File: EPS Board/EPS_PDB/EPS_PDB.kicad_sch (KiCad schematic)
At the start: 2 parts, among them J1 Conn_02x26_Odd_Even, J2 Conn_02x26_Odd_Even

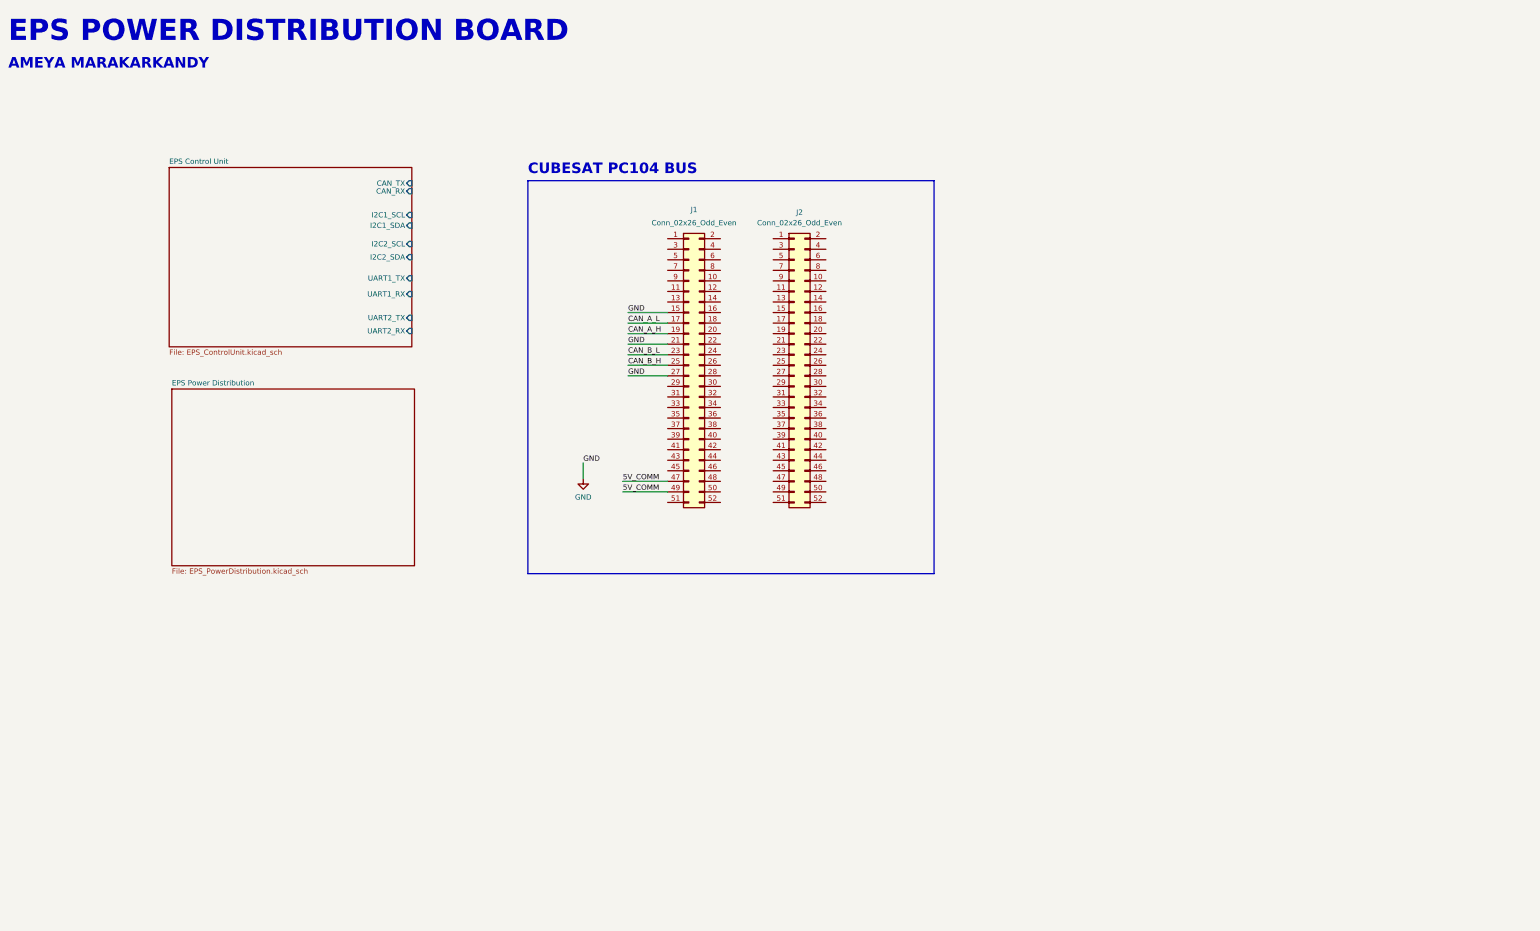
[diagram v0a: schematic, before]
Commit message: EPS PDB Board Schematic progress
Interfaces defined in EPS PDB board Schematic
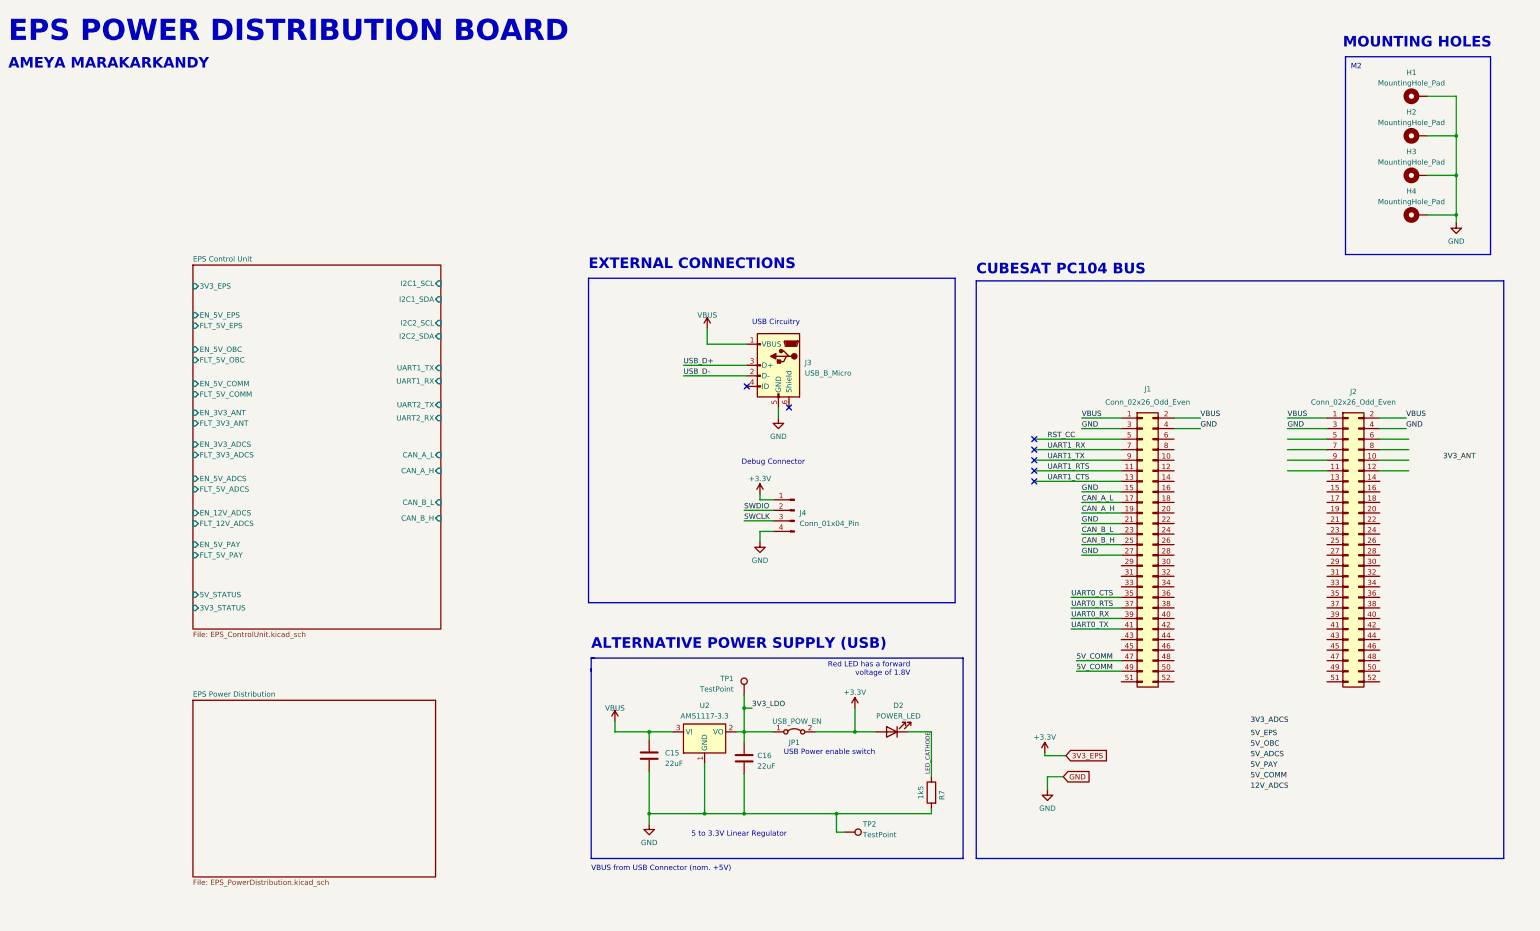
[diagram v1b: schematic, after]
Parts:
- added C15, C16: 22uF, symbol Device:C
- added D2: POWER_LED, symbol Device:LED
- added H1, H2, H3, H4: MountingHole_Pad, symbol Mechanical:MountingHole_Pad
- added J3: USB_B_Micro, symbol Connector:USB_B_Micro
- added J4: Conn_01x04_Pin, symbol Connector:Conn_01x04_Pin
- added JP1: USB_POW_EN, symbol Jumper:Jumper_2_Bridged
- added R7: 1k5, symbol Device:R
- added TP1, TP2: TestPoint, symbol Connector:TestPoint
- added U2: AMS1117-3.3, symbol Regulator_Linear:AMS1117-3.3
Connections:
- net GND: now also J1.3 (Pin_3), J1.4 (Pin_4), J2.3 (Pin_3), J2.4 (Pin_4), C15.2, C16.2, H1.1, H2.1, H3.1, H4.1, J3.5 (GND), J4.4 (Pin_4), R7.2, TP2.1, U2.1 (GND)
- net VBUS: now reaches J1.1 (Pin_1)
- net VBUS: now also J1.2 (Pin_2), J2.1 (Pin_1), J2.2 (Pin_2), C15.1, J3.1 (VBUS), U2.3 (VI)
- net UART1_RTS: now reaches J1.11 (Pin_11)
- net UART1_CTS: now reaches J1.13 (Pin_13)
- net UART0_CTS: now reaches J1.35 (Pin_35)
- net UART0_RTS: now reaches J1.37 (Pin_37)
- net UART0_RX: now reaches J1.39 (Pin_39)
- net UART0_TX: now reaches J1.41 (Pin_41)
- net RST_CC: now reaches J1.5 (Pin_5)
- net UART1_RX: now reaches J1.7 (Pin_7)
- net UART1_TX: now reaches J1.9 (Pin_9)
- new net +3.3V: D2.2 (A), J4.1 (Pin_1), JP1.2 (B)
- new net 3V3_LDO: C16.1, JP1.1 (A), TP1.1, U2.2 (VO)
- new net LED_CATHODE: D2.1 (K), R7.1
- new net SWCLK: J4.3 (Pin_3)
- new net SWDIO: J4.2 (Pin_2)
- new net USB_D+: J3.3 (D+)
- new net USB_D-: J3.2 (D-)
- no-connect marks 0 -> 7
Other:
- sheet EPS Control Unit ports: added 3V3_EPS, 3V3_STATUS, 5V_STATUS, CAN_A_H, CAN_A_L, CAN_B_H, CAN_B_L, EN_12V_ADCS, EN_3V3_ADCS, EN_3V3_ANT, EN_5V_ADCS, EN_5V_COMM, EN_5V_EPS, EN_5V_OBC, EN_5V_PAY, FLT_12V_ADCS, FLT_3V3_ADCS, FLT_3V3_ANT, FLT_5V_ADCS, FLT_5V_COMM, FLT_5V_EPS, FLT_5V_OBC, FLT_5V_PAY; removed CAN_RX, CAN_TX
- note added: "5 to 3.3V Linear Regulator"
- note added: "ALTERNATIVE POWER SUPPLY (USB)"
- note added: "Debug Connector"
- note added: "EXTERNAL CONNECTIONS"
- note added: "M2"
- note added: "MOUNTING HOLES"
- note added: "Red LED has a forward voltage of 1.8V"
- note added: "USB Circuitry"
- note added: "USB Power enable switch"
- note added: "VBUS from USB Connector (nom. +5V)"
- moved on the sheet: J1, J2

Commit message: EPS PDB Schematic Progress
Assigned STM32 GPIO pins
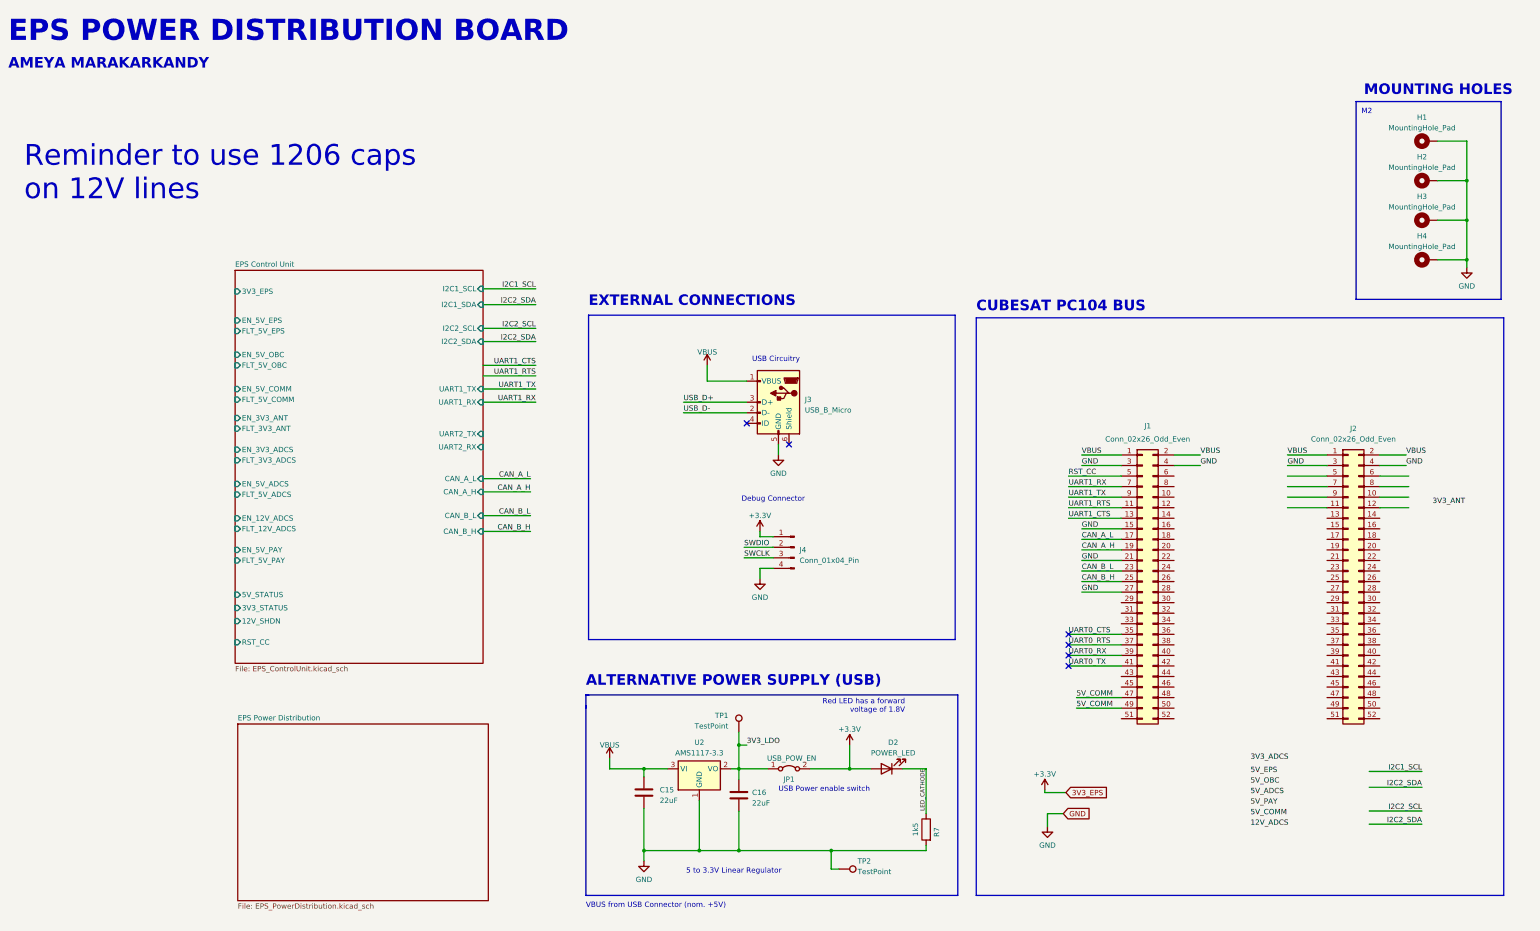
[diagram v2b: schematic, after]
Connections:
- no-connect marks 7 -> 6
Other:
- sheet EPS Control Unit ports: added 12V_SHDN, RST_CC; removed none
- note added: "Reminder to use 1206 caps on 12V lines"
- moved on the sheet: C15, C16, D2, H1, H2, H3, H4, J1, J2, J3, J4, JP1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

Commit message: Fixed libraries and updated schematic accordingly
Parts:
- renumbered C15 to C17, C16 to C18, D2 to D3, H1 to H5, H2 to H6, H3 to H7, H4 to H8, J4 to J5, J3 to J6, JP1 to JP2, R7 to R15, TP1 to TP3, TP2 to TP4, U2 to U6

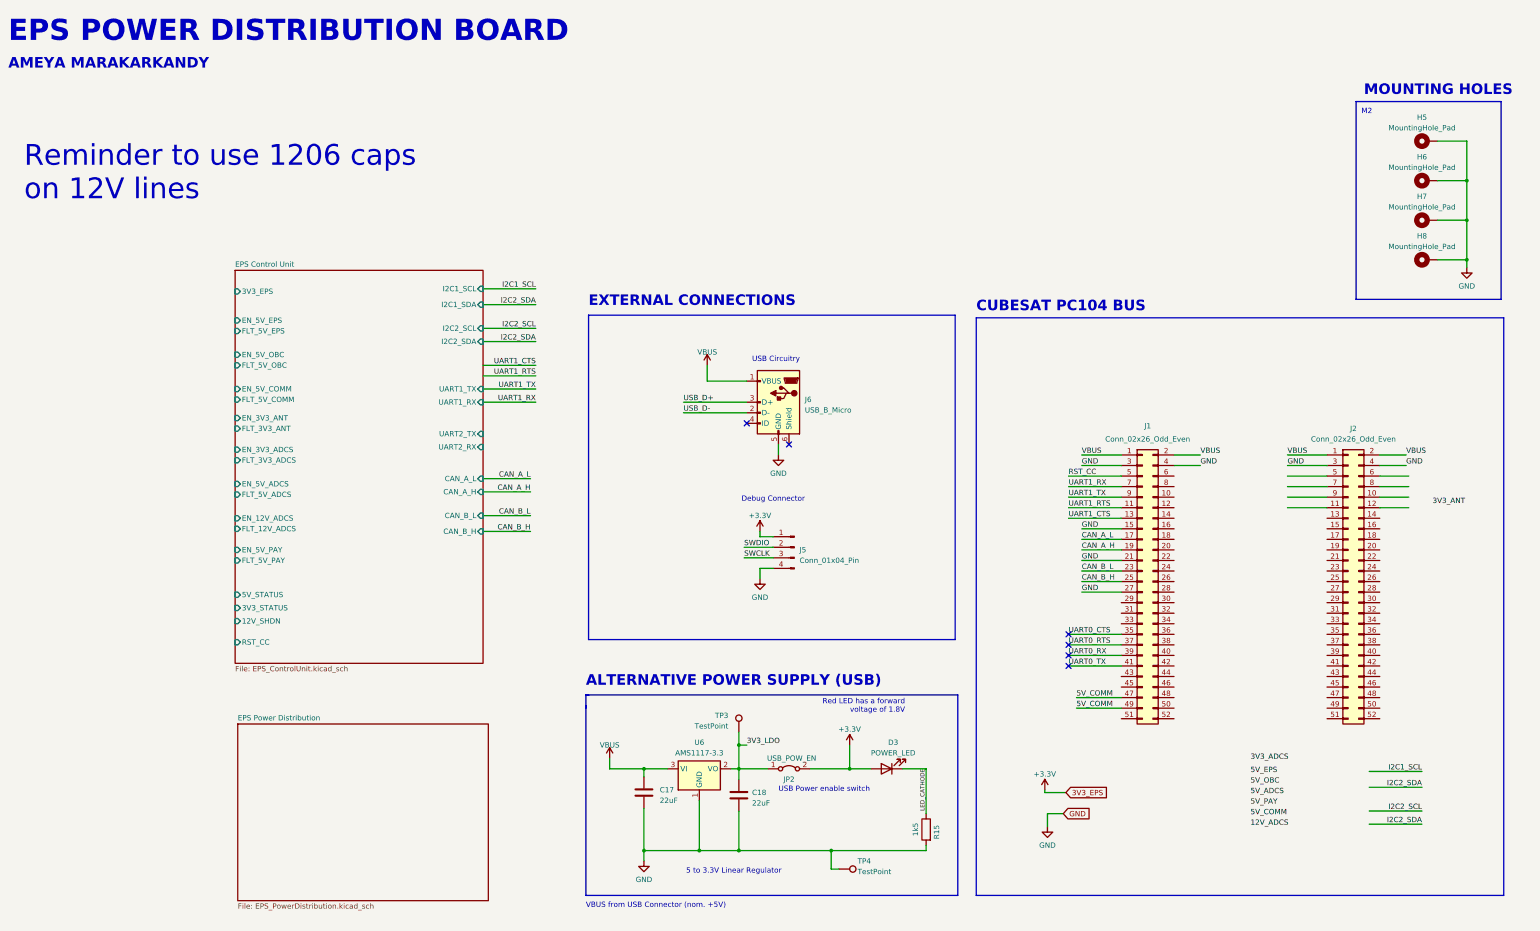
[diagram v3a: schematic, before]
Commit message: Added PCB dxf outline
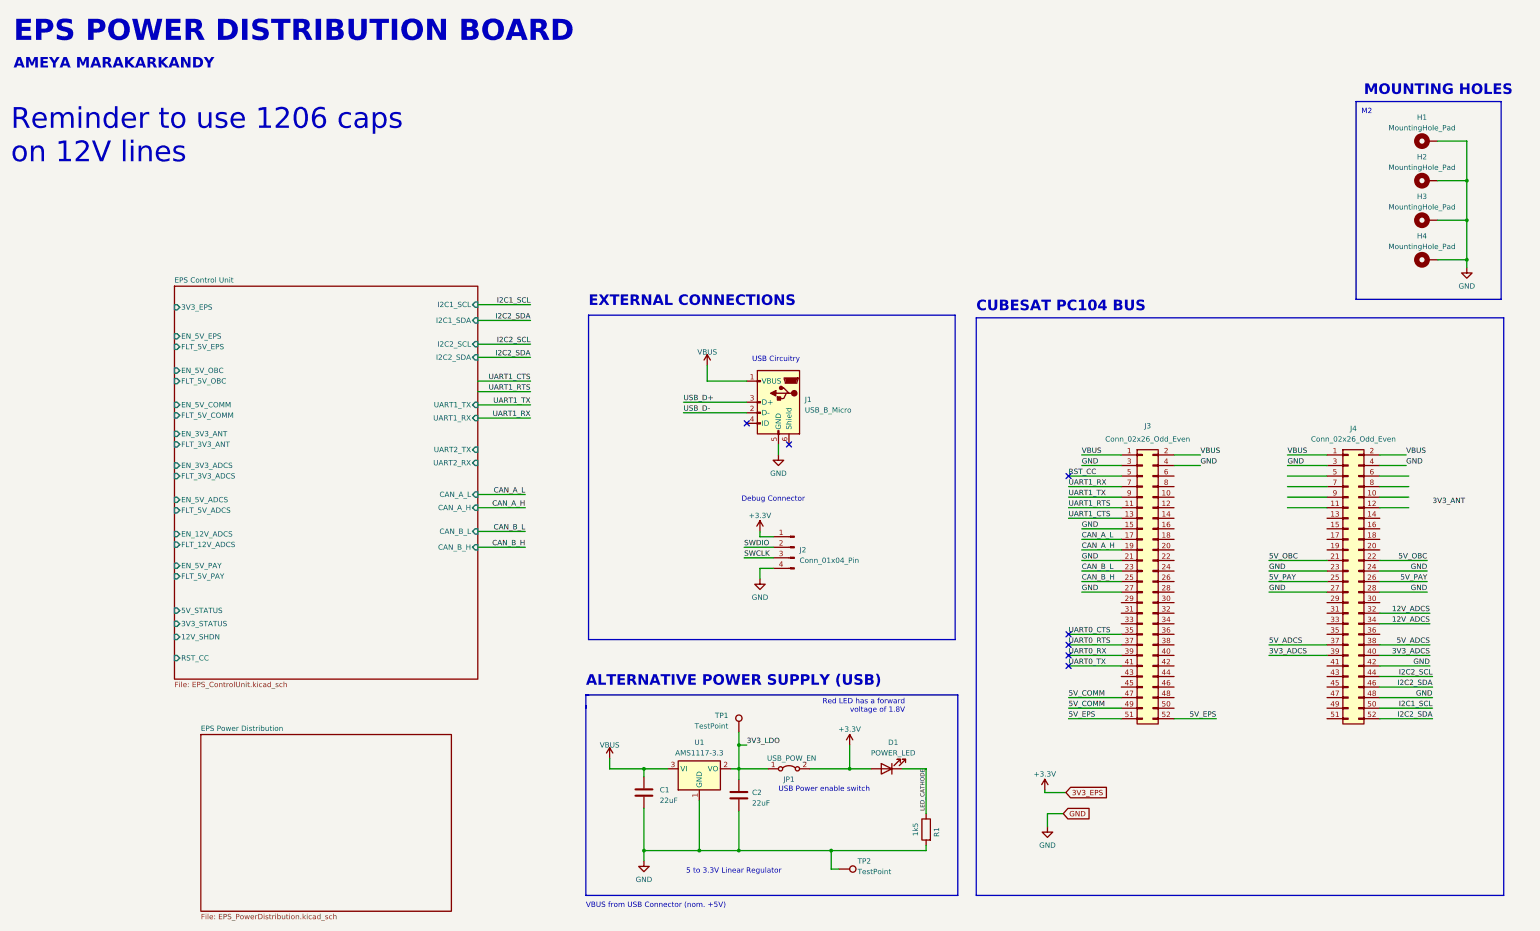
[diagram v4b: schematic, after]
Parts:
- renumbered C17 to C1, C18 to C2, D3 to D1, H5 to H1, H6 to H2, H7 to H3, H8 to H4, J6 to J1, J5 to J2, J1 to J3, J2 to J4, JP2 to JP1, R15 to R1, TP3 to TP1, TP4 to TP2, U6 to U1
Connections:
- net 12V_ADCS: now also J4.32 (Pin_32), J4.34 (Pin_34)
- net 3V3_ADCS: now also J4.39 (Pin_39), J4.40 (Pin_40)
- net 5V_ADCS: now also J4.37 (Pin_37), J4.38 (Pin_38)
- net 5V_EPS: now also J3.51 (Pin_51), J3.52 (Pin_52)
- net 5V_OBC: now also J4.21 (Pin_21), J4.22 (Pin_22)
- net 5V_PAY: now also J4.25 (Pin_25), J4.26 (Pin_26)
- net GND: now also J4.23 (Pin_23), J4.24 (Pin_24), J4.27 (Pin_27), J4.28 (Pin_28), J4.42 (Pin_42), J4.48 (Pin_48)
- net I2C1_SCL: now also J4.50 (Pin_50)
- net I2C2_SCL: now also J4.44 (Pin_44)
- net I2C2_SDA: now also J4.46 (Pin_46), J4.52 (Pin_52)
- no-connect marks 6 -> 7

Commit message: completed CAN transceiver switching circuit
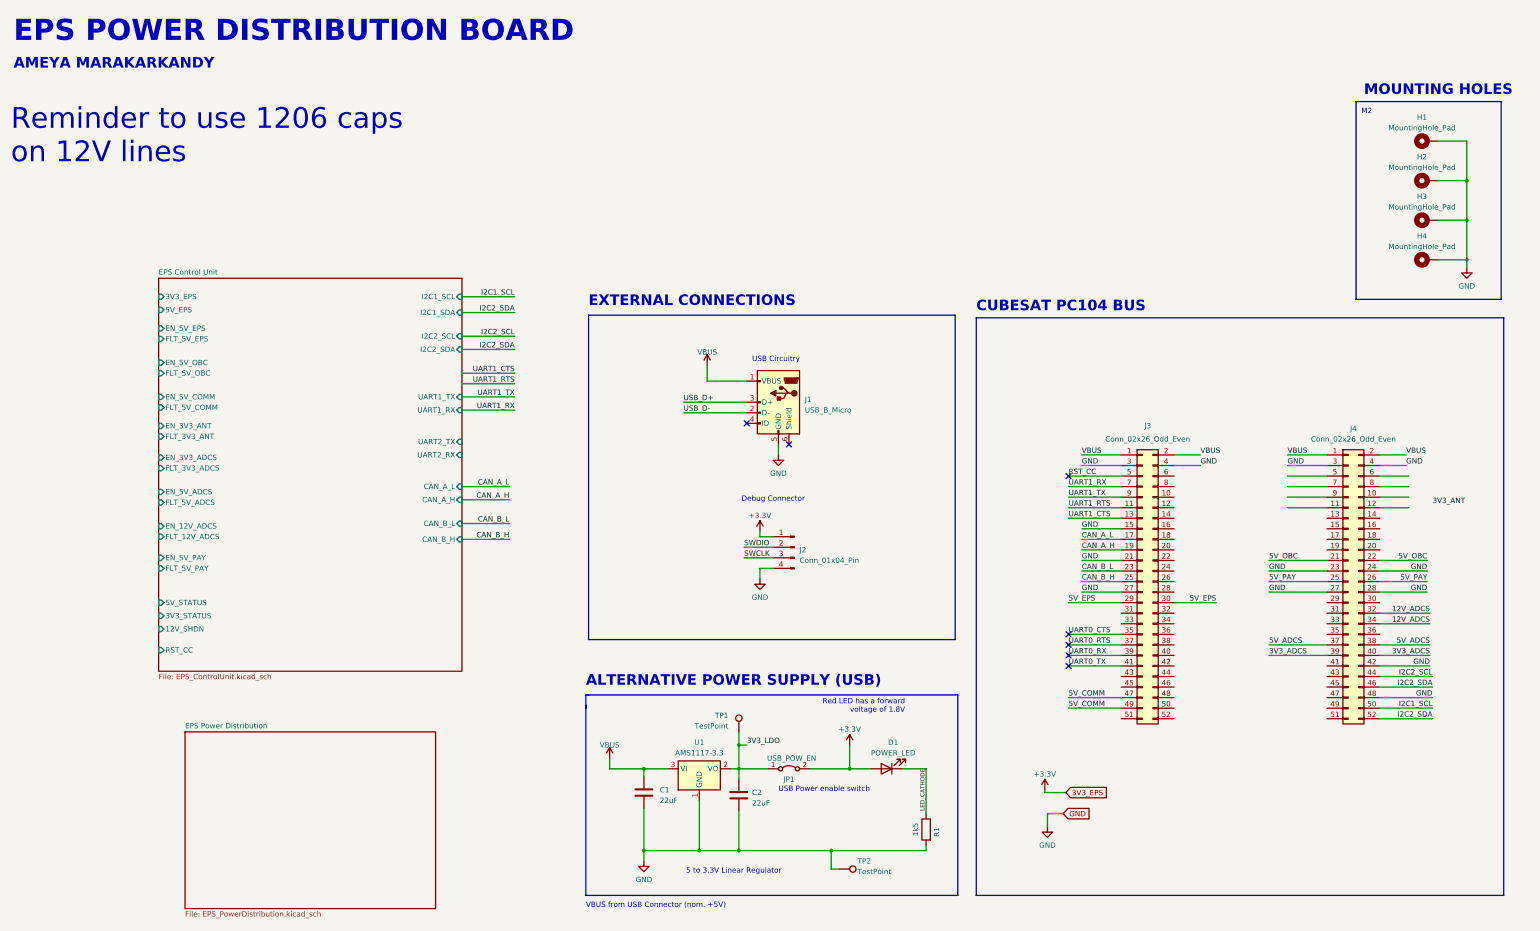
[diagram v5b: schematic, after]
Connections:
- net 5V_EPS: now also J3.29 (Pin_29), J3.30 (Pin_30); no longer J3.51 (Pin_51), J3.52 (Pin_52)
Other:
- sheet EPS Control Unit ports: added 5V_EPS; removed none
